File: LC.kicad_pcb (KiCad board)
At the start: 2 copper layers, 60 x 65 mm, 81 parts, among them J1 INPUT+, J10 DISPLAY, J11 MODE_BUTTON, J12 CAL_BUTTON, J2 INPUT-, J3 Barrel_Jack, J4 EXT_CLK, J5 CLKSRC, J6 SIGSRC, J7 EXT_SIG, J8 Conn_01x06_Male, J9 PROG, Q1 BC817, Q2 BC817, SW1 RESET_BTN, U1 Omron_G2V, U10 74HC590PW,118, U11 74HCS251, U12 AVR32DB28x-xSO, U2 L7805, U3 74AHC1G04, U4 Omron_G2E, U5 74AHC1G14, U6 74AHC1G04, U7 LM311, U8 74AUC1G74, U9 74AUC2G125, Y1 10MHz

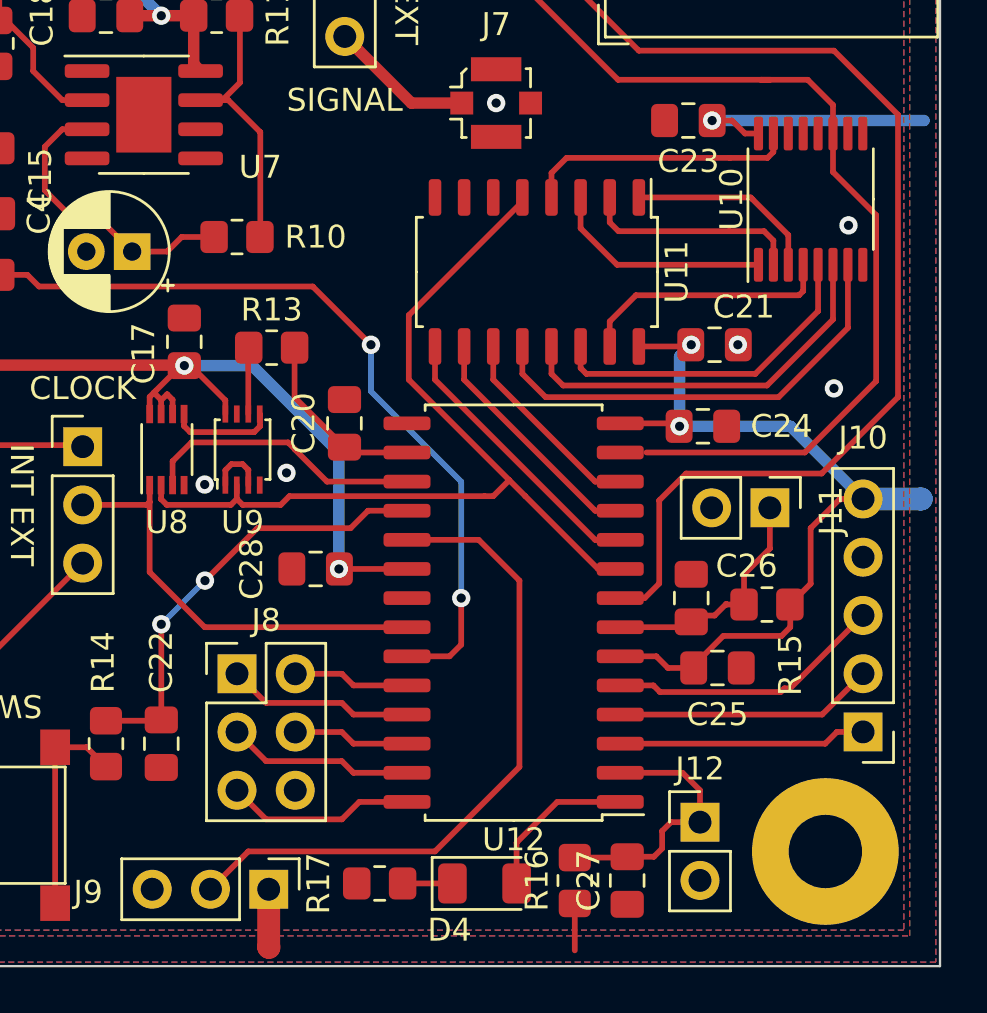
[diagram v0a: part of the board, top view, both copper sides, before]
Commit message: update display connector
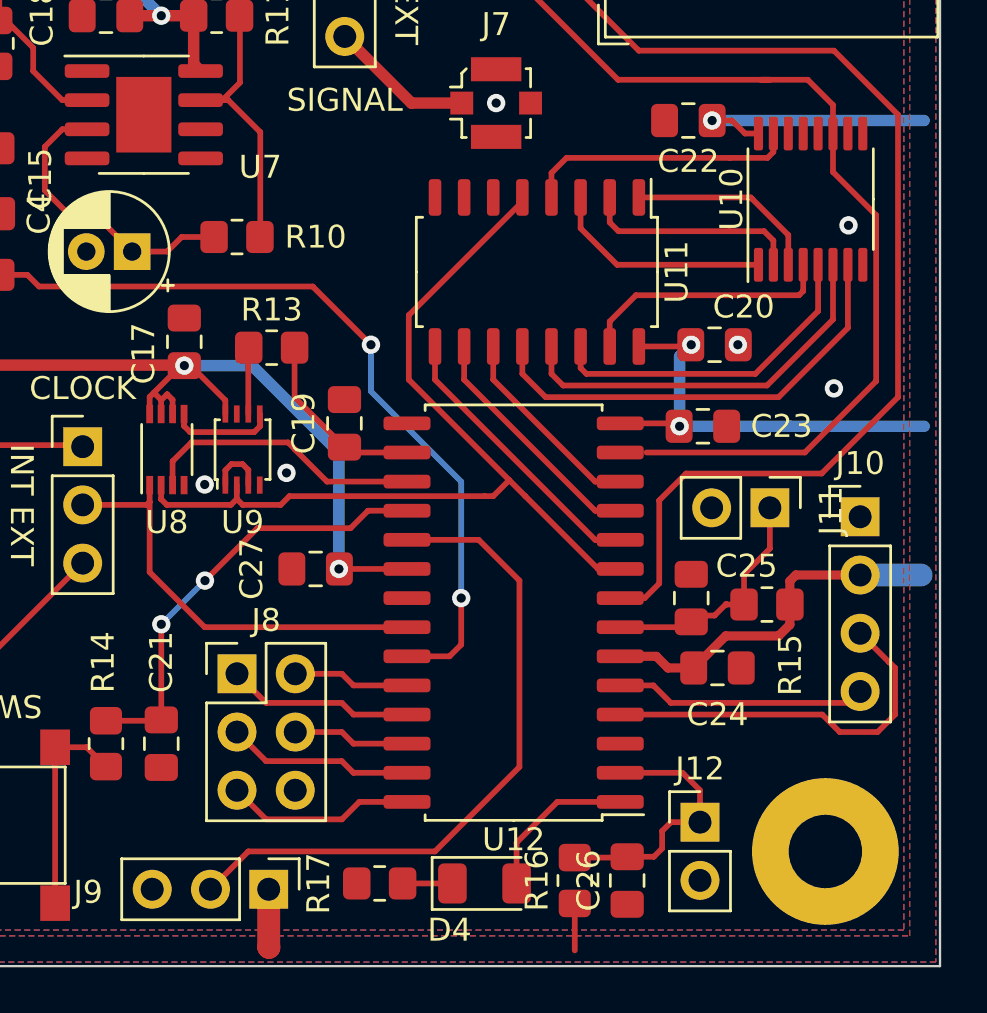
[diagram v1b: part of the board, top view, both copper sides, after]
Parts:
- J10: footprint Connector_PinHeader_2.54mm:PinHeader_1x05_P2.54mm_Vertical -> Connector_PinHeader_2.54mm:PinHeader_1x04_P2.54mm_Vertical
- moved J10 9.38 mm to (191.5, 80.4), turned to 0 degrees
- renumbered C20 to C19, C21 to C20, C22 to C21, C23 to C22, C24 to C23, C25 to C24, C26 to C25, C27 to C26, C28 to C27
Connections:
- J10 pad 1: /DISP/SS -> GND
- J10 pad 2: /DISP/SDA -> +5V
- J10 pad 3: /DISP/SDC -> /DISP/SDA
- J10 pad 4: GND -> /DISP/SDC
- U12 pad 3: /DISP/SS -> /UNUSED_6
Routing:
- net /DISP/SS: track 10.8 -> 0.00 mm
- net /DISP/SDA: track 11.3 -> 16.8 mm
- net /DISP/SDC: track 12.1 -> 11.0 mm
- net +5V: track 186.7 -> 185.7 mm

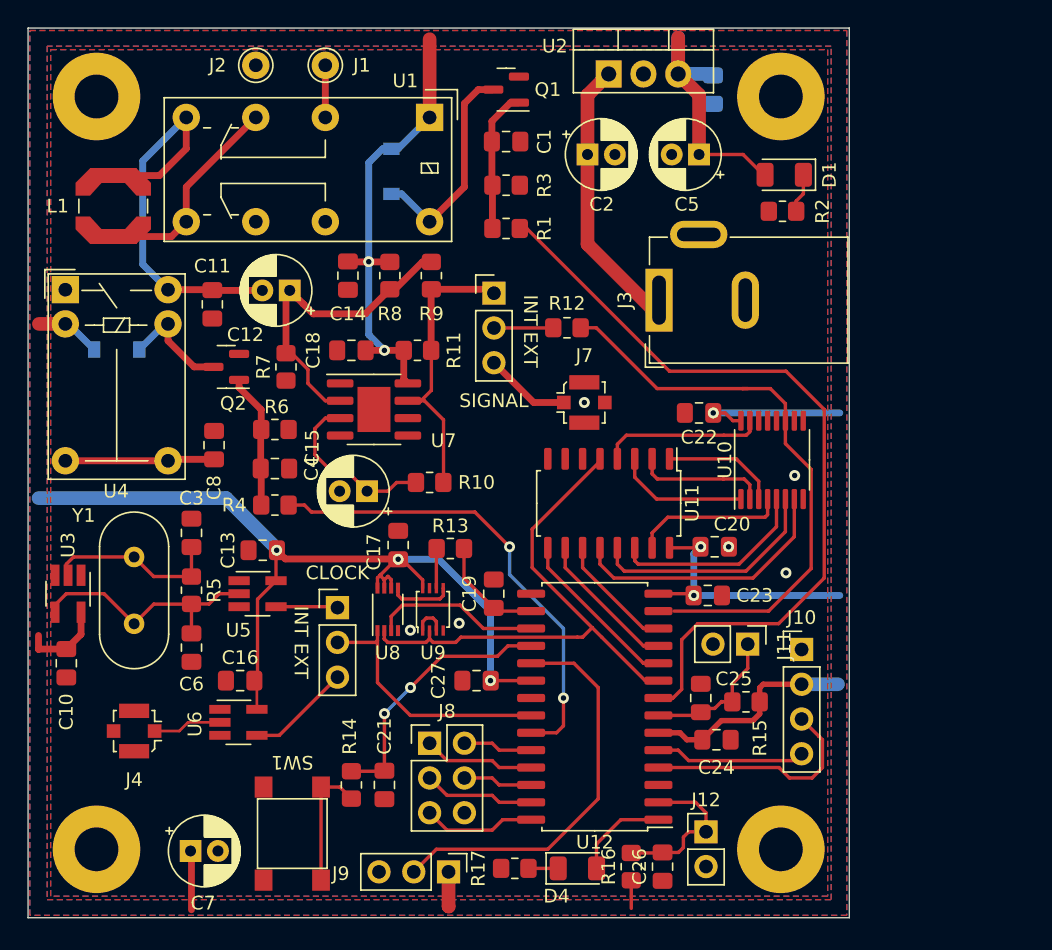
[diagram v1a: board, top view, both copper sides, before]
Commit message: Unused IO to connector and LCD connector
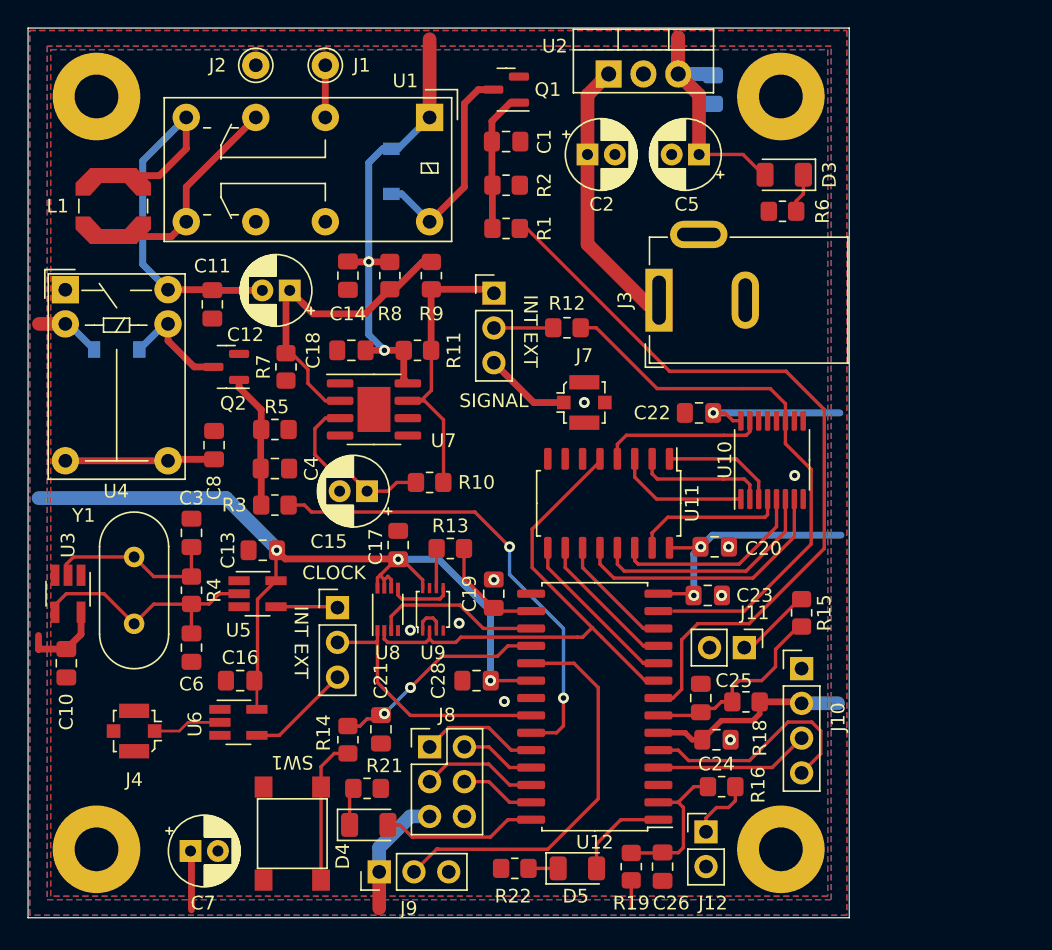
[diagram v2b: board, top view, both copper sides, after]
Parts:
- added D4: LED, LED_SMD:LED_1206_3216Metric, F.Cu at (159.9, 93.2)
- added R15: 1k, Resistor_SMD:R_0805_2012Metric_Pad1.20x1.40mm_HandSolder, F.Cu at (191.5, 77.7)
- added R16: 1k, Resistor_SMD:R_0805_2012Metric_Pad1.20x1.40mm_HandSolder, F.Cu at (185.7, 90.4)
- added R21: 470R, Resistor_SMD:R_0805_2012Metric_Pad1.20x1.40mm_HandSolder, F.Cu at (159.8, 90.6)
- J11: value MODE_BUTTON -> ENTER_BUTTON
- J12: value CAL_BUTTON -> UP_BUTTON
- J8: value Conn_01x06_Male -> UNUSED
- R18: renamed from R15; value 10k-DNP -> 10k
- R19: renamed from R16; value 10k-DNP -> 10k
- moved J9 5.06 mm to (160.7, 96.6), turned to 90 degrees
- moved C21 4.07 mm to (160.8, 86.2)
- moved R14 3.31 mm to (158.4, 87.0)
- moved J10 1.40 mm to (191.5, 81.8)
- moved J11 0.36 mm to (187.3, 80.3)
- moved J8 0.27 mm to (164.3, 87.5)
- renumbered C27 to C28, D2 to D1, D3 to D2, D1 to D3, D4 to D5, R3 to R2, R17 to R22, R4 to R3, R5 to R4, R6 to R5, R2 to R6
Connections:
- C25 pad 2: /MOD_SEL -> /BTN_ENTER
- C26 pad 2: /CAL_SEL -> /BTN_ITER
- J11 pad 1: /MOD_SEL -> Net-(J11-Pad1)
- J12 pad 1: /CAL_SEL -> Net-(J12-Pad1)
- J8 pad 1: /UNUSED_2 -> /UNUSED_1
- J8 pad 2: /UNUSED_1 -> /UNUSED_2
- J8 pad 3: /UNUSED_4 -> /UNUSED_3
- J8 pad 4: /UNUSED_3 -> /UNUSED_4
- J8 pad 5: /UNUSED_5 -> +5V
- R18 pad 2: /MOD_SEL -> /BTN_ENTER
- R19 pad 2: /CAL_SEL -> /BTN_ITER
- U12 pad 2: /CAL_SEL -> /BTN_ITER
- U12 pad 28: /UNUSED_5 -> Net-(U12-Pad28)
- U12 pad 3: /UNUSED_6 -> unconnected-(U12-Pad3)
- U12 pad 7: /MOD_SEL -> /BTN_ENTER
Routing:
- net /BTN_ENTER: track 0.00 -> 14.5 mm
- net /CAL_SEL: track 11.7 -> 0.00 mm
- net /BTN_ITER: track 0.00 -> 11.5 mm
- net Net-(U12-Pad28): track 0.00 -> 11.4 mm
- net /MOD_SEL: track 10.5 -> 0.00 mm
- net /UNUSED_5: track 8.26 -> 0.00 mm
- net /DISP/SDC: track 11.0 -> 17.3 mm
- net Net-(J11-Pad1): track 0.00 -> 5.65 mm
- net /DISP/SDA: track 16.8 -> 11.4 mm
- net +5V: track 185.7 -> 191.0 mm
- net Net-(J12-Pad1): track 0.00 -> 4.71 mm
- net /~{RESET}: track 19.4 -> 15.5 mm
- net /UNUSED_1: track 5.09 -> 8.69 mm
- net /UNUSED_3: track 5.09 -> 8.59 mm
- net Net-(D4-Pad1): track 0.00 -> 2.78 mm
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
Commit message: update gitignore and init code
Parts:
- added TP1: TestPoint, TestPoint:TestPoint_THTPad_1.0x1.0mm_Drill0.5mm, B.Cu at (175.3, 94.8)
- moved D5 0.68 mm to (175.4, 97.0)
- moved R20 0.68 mm to (170.8, 97.0)
- renumbered C28 to C27, R18 to R17, R19 to R18, R21 to R19, R22 to R20
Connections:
- net Net-(U12-Pad1) renamed /LED_2
- net Net-(U12-Pad28) renamed /LED_1
- U12 pad 3: unconnected-(U12-Pad3) -> /UNUSED_5
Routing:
- net /UNUSED_5: track 0.00 -> 7.83 mm
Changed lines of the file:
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@@
   (net 57 "/DISP{slash}SDA")
   (net 58 "/DISP{slash}SDC")
-  (net 59 "Net-(U12-Pad1)")
+  (net 59 "/LED_1")
   (net 60 "/UNUSED_1")
   (net 61 "/UNUSED_2")
@@
   (net 64 "/BTN_ENTER")
   (net 65 "Net-(D3-Pad1)")
-  (net 66 "Net-(U12-Pad28)")
+  (net 66 "/LED_2")
   (net 67 "Net-(D5-Pad1)")
   (net 68 "Net-(J11-Pad1)")
   (net 69 "Net-(J12-Pad1)")
   (net 70 "/BTN_ITER")
-  (net 71 "unconnected-(U12-Pad3)")
+  (net 71 "/UNUSED_5")
   (footprint "Resistor_SMD:R_0805_2012Metric_Pad1.20x1.40mm_HandSolder" (layer "F.Cu")
     (at 159.766 90.551)
@@
     (property "Sheetname" "")
     (attr smd)
-    (fp_text reference "R21" (at 1.27 -1.65) (layer "F.SilkS")
+    (fp_text reference "R19" (at 1.27 -1.65) (layer "F.SilkS")
       (effects (font (size 1 1) (thickness 0.15)))
     )
@@
     (property "Sheetname" "")
     (attr smd)
-    (fp_text reference "C28" (at -2.794 0 90) (layer "F.SilkS")
+    (fp_text reference "C27" (at -2.794 0 90) (layer "F.SilkS")
       (effects (font (size 1 1) (thickness 0.15)))
     )
@@
     (property "Sheetname" "")
     (attr smd)
-    (fp_text reference "R19" (at -2.667 0 180) (layer "F.SilkS")
+    (fp_text reference "R18" (at -2.667 0 180) (layer "F.SilkS")
       (effects (font (size 1 1) (thickness 0.15)))
     )
@@
       (net 41 "Net-(D4-Pad1)") (pinfunction "K") (pintype "passive"))
     (pad "2" smd roundrect (at 1.4 0) (size 1.25 1.75) (layers "F.Cu" "F.Paste" "F.Mask") (roundrect_rratio 0.2)
-      (net 66 "Net-(U12-Pad28)") (pinfunction "A") (pintype "passive"))
+      (net 59 "/LED_1") (pinfunction "A") (pintype "passive"))
     (model "${KICAD6_3DMODEL_DIR}/LED_SMD.3dshapes/LED_1206_3216Metric.wrl"
       (offset (xyz 0 0 0))
@@
   )
   (footprint "LED_SMD:LED_1206_3216Metric" (layer "F.Cu")
-    (at 175.133 96.393)
+    (at 175.387 97.028)
     (descr "LED SMD 1206 (3216 Metric), square (rectangular) end terminal, IPC_7351 nominal, (Body size source: http://www.tortai-tech.com/upload/download/2011102023233369053.pdf), generated with kicad-footprint-generator")
     (tags "LED")
@@
       (net 67 "Net-(D5-Pad1)") (pinfunction "K") (pintype "passive"))
     (pad "2" smd roundrect (at 1.4 0) (size 1.25 1.75) (layers "F.Cu" "F.Paste" "F.Mask") (roundrect_rratio 0.2)
-      (net 59 "Net-(U12-Pad1)") (pinfunction "A") (pintype "passive"))
+      (net 66 "/LED_2") (pinfunction "A") (pintype "passive"))
     (model "${KICAD6_3DMODEL_DIR}/LED_SMD.3dshapes/LED_1206_3216Metric.wrl"
       (offset (xyz 0 0 0))
@@
   )
   (footprint "Resistor_SMD:R_0805_2012Metric_Pad1.20x1.40mm_HandSolder" (layer "F.Cu")
-    (at 170.561 96.393 180)
+    (at 170.815 97.028 180)
     (descr "Resistor SMD 0805 (2012 Metric), square (rectangular) end terminal, IPC_7351 nominal with elongated pad for handsoldering. (Body size source: IPC-SM-782 page 72, https://www.pcb-3d.com/wordpress/wp-content/uploads/ipc-sm-782a_amendment_1_and_2.pdf), generated with kicad-footprint-generator")
     (tags "resistor handsolder")
@@
     (property "Sheetname" "")
     (attr smd)
-    (fp_text reference "R22" (at 0.127 -2.032 180) (layer "F.SilkS")
+    (fp_text reference "R20" (at 0.127 -2.032 180) (layer "F.SilkS")
       (effects (font (size 1 1) (thickness 0.15)))
     )
@@
     (property "Sheetname" "")
     (attr smd)
-    (fp_text reference "U12" (at 0 -9.9) (layer "F.SilkS")
+    (fp_text reference "U12" (at 5.207 -10.16) (layer "F.SilkS")
       (effects (font (size 1 1) (thickness 0.15)))
     )
@@
     (fp_line (start -2.75 -8.95) (end 3.75 -8.95) (layer "F.Fab") (width 0.1))
     (pad "1" smd roundrect (at -4.65 -8.255 180) (size 2.05 0.6) (layers "F.Cu" "F.Paste" "F.Mask") (roundrect_rratio 0.25)
-      (net 59 "Net-(U12-Pad1)") (pinfunction "PA7") (pintype "bidirectional"))
+      (net 66 "/LED_2") (pinfunction "PA7") (pintype "bidirectional"))
     (pad "2" smd roundrect (at -4.65 -6.985 180) (size 2.05 0.6) (layers "F.Cu" "F.Paste" "F.Mask") (roundrect_rratio 0.25)
       (net 70 "/BTN_ITER") (pinfunction "PC0") (pintype "bidirectional"))
     (pad "3" smd roundrect (at -4.65 -5.715 180) (size 2.05 0.6) (layers "F.Cu" "F.Paste" "F.Mask") (roundrect_rratio 0.25)
-      (net 71 "unconnected-(U12-Pad3)") (pinfunction "PC1") (pintype "bidirectional"))
+      (net 71 "/UNUSED_5") (pinfunction "PC1") (pintype "bidirectional"))
     (pad "4" smd roundrect (at -4.65 -4.445 180) (size 2.05 0.6) (layers "F.Cu" "F.Paste" "F.Mask") (roundrect_rratio 0.25)
       (net 57 "/DISP{slash}SDA") (pinfunction "PC2") (pintype "bidirectional"))
@@
       (net 63 "/UNUSED_4") (pinfunction "PA5") (pintype "bidirectional"))
     (pad "28" smd roundrect (at 4.65 -8.255 180) (size 2.05 0.6) (layers "F.Cu" "F.Paste" "F.Mask") (roundrect_rratio 0.25)
-      (net 66 "Net-(U12-Pad28)") (pinfunction "PA6") (pintype "bidirectional"))
+      (net 59 "/LED_1") (pinfunction "PA6") (pintype "bidirectional"))
     (model "${KICAD6_3DMODEL_DIR}/Package_SO.3dshapes/SOIC-28W_7.5x17.9mm_P1.27mm.wrl"
       (offset (xyz 0 0 0))
@@
     (property "Sheetname" "")
     (attr smd)
-    (fp_text reference "R18" (at -1.016 -2.64 270) (layer "F.SilkS")
+    (fp_text reference "R17" (at -1.016 -2.64 270) (layer "F.SilkS")
       (effects (font (size 1 1) (thickness 0.15)))
     )
@@
     )
   )
+  (footprint "TestPoint:TestPoint_THTPad_1.0x1.0mm_Drill0.5mm" (layer "B.Cu")
+    (at 175.3108 94.8436 180)
+    (descr "THT rectangular pad as test Point, square 1.0mm side length, hole diameter 0.5mm")
+    (tags "test point THT pad rectangle square")
+    (property "Sheetfile" "LC.kicad_sch")
+    (property "Sheetname" "")
+    (attr exclude_from_pos_files)
+    (fp_text reference "TP1" (at 2.6162 -0.1524) (layer "B.SilkS")
+      (effects (font (size 1 1) (thickness 0.15)) (justify mirror))
+    )
+    (fp_text value "TestPoint" (at 0 -1.55) (layer "B.Fab")
+      (effects (font (size 1 1) (thickness 0.15)) (justify mirror))
+    )
+    (fp_text user "${REFERENCE}" (at 0 1.45) (layer "B.Fab")
+      (effects (font (size 1 1) (thickness 0.15)) (justify mirror))
+    )
+    (fp_line (start -0.7 0.7) (end 0.7 0.7) (layer "B.SilkS") (width 0.12))
+    (fp_line (start -0.7 -0.7) (end -0.7 0.7) (layer "B.SilkS") (width 0.12))
+    (fp_line (start 0.7 0.7) (end 0.7 -0.7) (layer "B.SilkS") (width 0.12))
+    (fp_line (start 0.7 -0.7) (end -0.7 -0.7) (layer "B.SilkS") (width 0.12))
+    (fp_line (start 1 -1) (end 1 1) (layer "B.CrtYd") (width 0.05))
+    (fp_line (start -1 1) (end 1 1) (layer "B.CrtYd") (width 0.05))
+    (fp_line (start -1 1) (end -1 -1) (layer "B.CrtYd") (width 0.05))
+    (fp_line (start 1 -1) (end -1 -1) (layer "B.CrtYd") (width 0.05))
+    (pad "1" thru_hole rect (at 0 0 180) (size 1 1) (drill 0.5) (layers *.Cu *.Mask)
+      (net 71 "/UNUSED_5") (pinfunction "1") (pintype "passive"))
+  )
   (footprint "Diode_SMD:D_SOD-123" (layer "B.Cu")
     (at 141.478 58.486)
@@
   (segment (start 183.261 88.519) (end 187.706 88.519) (width 0.25) (layer "F.Cu") (net 58))
   (segment (start 181.053 87.757) (end 182.499 87.757) (width 0.25) (layer "F.Cu") (net 58))
-  (segment (start 176.53 96.39) (end 176.533 96.393) (width 0.25) (layer "F.Cu") (net 59))
-  (segment (start 178.308 92.837) (end 176.53 94.615) (width 0.25) (layer "F.Cu") (net 59))
-  (segment (start 181.053 92.837) (end 178.308 92.837) (width 0.25) (layer "F.Cu") (net 59))
-  (segment (start 176.53 94.615) (end 176.53 96.39) (width 0.25) (layer "F.Cu") (net 59))
+  (segment (start 162.179 93.218) (end 163.068 94.107) (width 0.25) (layer "F.Cu") (net 59))
+  (segment (start 163.068 94.107) (end 168.783 94.107) (width 0.25) (layer "F.Cu") (net 59))
+  (segment (start 170.053 92.837) (end 171.753 92.837) (width 0.25) (layer "F.Cu") (net 59))
+  (segment (start 168.783 94.107) (end 170.053 92.837) (width 0.25) (layer "F.Cu") (net 59))
+  (segment (start 161.293 93.218) (end 162.179 93.218) (width 0.25) (layer "F.Cu") (net 59))
   (segment (start 164.338 87.518) (end 164.338 87.503) (width 0.25) (layer "F.Cu") (net 60))
   (segment (start 165.735 86.106) (end 168.656 86.106) (width 0.25) (layer "F.Cu") (net 60))
@@
   (segment (start 191.119 47.641) (end 191.646 47.114) (width 0.25) (layer "F.Cu") (net 65))
   (segment (start 191.119 48.387) (end 191.119 47.641) (width 0.25) (layer "F.Cu") (net 65))
-  (segment (start 162.179 93.218) (end 163.068 94.107) (width 0.25) (layer "F.Cu") (net 66))
-  (segment (start 163.068 94.107) (end 168.783 94.107) (width 0.25) (layer "F.Cu") (net 66))
-  (segment (start 170.053 92.837) (end 171.753 92.837) (width 0.25) (layer "F.Cu") (net 66))
-  (segment (start 168.783 94.107) (end 170.053 92.837) (width 0.25) (layer "F.Cu") (net 66))
-  (segment (start 161.293 93.218) (end 162.179 93.218) (width 0.25) (layer "F.Cu") (net 66))
-  (segment (start 173.733 96.393) (end 171.561 96.393) (width 0.25) (layer "F.Cu") (net 67))
+  (segment (start 176.787 97.028) (end 176.787 94.739) (width 0.25) (layer "F.Cu") (net 66))
+  (segment (start 178.689 92.837) (end 181.053 92.837) (width 0.25) (layer "F.Cu") (net 66))
+  (segment (start 176.787 94.739) (end 178.689 92.837) (width 0.25) (layer "F.Cu") (net 66))
+  (segment (start 171.815 97.028) (end 173.987 97.028) (width 0.25) (layer "F.Cu") (net 67))
   (segment (start 187.833 80.264) (end 187.33 80.264) (width 0.25) (layer "F.Cu") (net 68))
   (segment (start 191.516 76.724) (end 191.373 76.724) (width 0.25) (layer "F.Cu") (net 68))
@@
   (segment (start 183.642 90.424) (end 184.674 90.424) (width 0.25) (layer "F.Cu") (net 70))
   (segment (start 179.07 95.266) (end 181.3185 95.266) (width 0.25) (layer "F.Cu") (net 70))
+  (segment (start 175.3108 94.488) (end 179.5018 90.297) (width 0.25) (layer "F.Cu") (net 71))
+  (segment (start 179.5018 90.297) (end 181.053 90.297) (width 0.25) (layer "F.Cu") (net 71))
+  (segment (start 175.3108 94.8436) (end 175.3108 94.488) (width 0.25) (layer "F.Cu") (net 71))
   (zone (net 4) (net_name "GND") (layers F&B.Cu) (hatch edge 0.508)
     (connect_pads (clearance 0))
